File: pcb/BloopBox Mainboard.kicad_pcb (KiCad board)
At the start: 4 copper layers, 65 x 44 mm, 58 parts, among them J1 ExtLED, J2 SPKR, J3 Raspberry_Pi, J4 I2C, J5 NFC-Module, J6 GPIO, J7 TailBoard, J8 PROG, Q1 2N7002, Q2 2N7002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

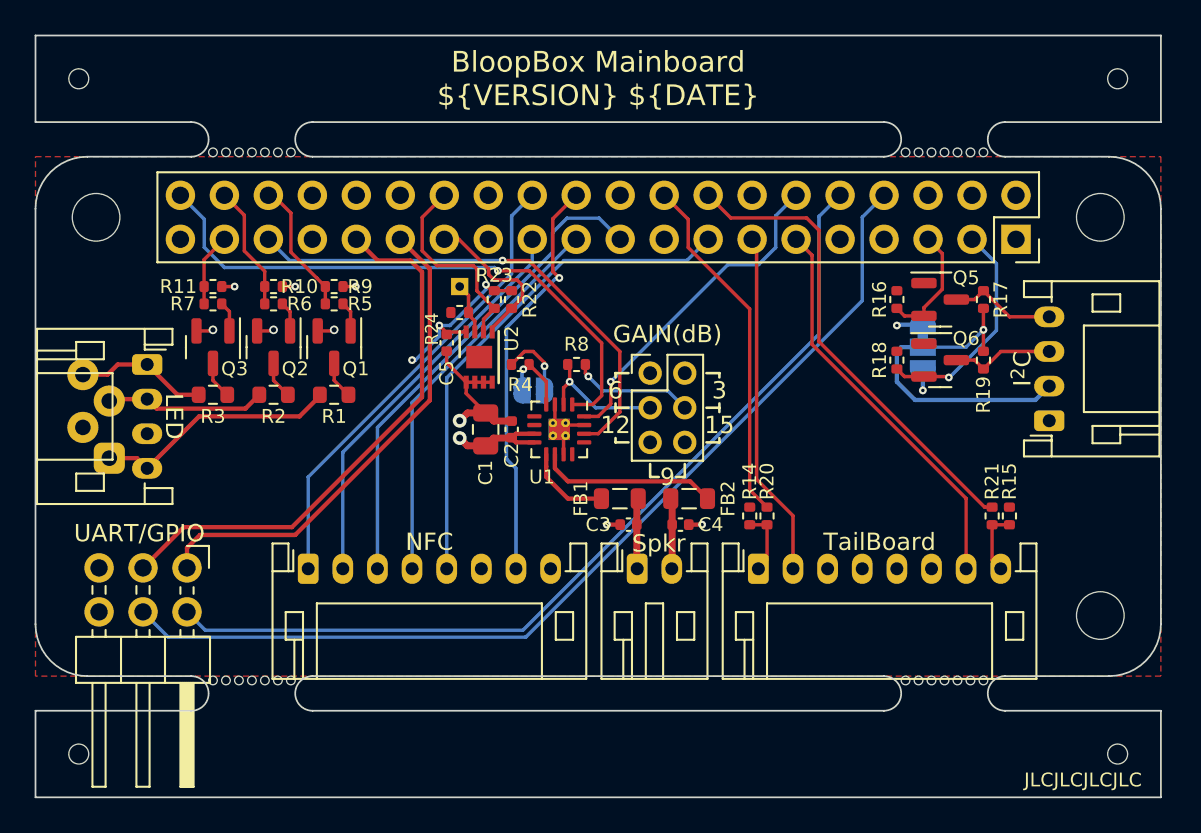
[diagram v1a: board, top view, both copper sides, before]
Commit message: feat!: remove RGB LED
remove the RGB LED facilities since we're using I2C for that now
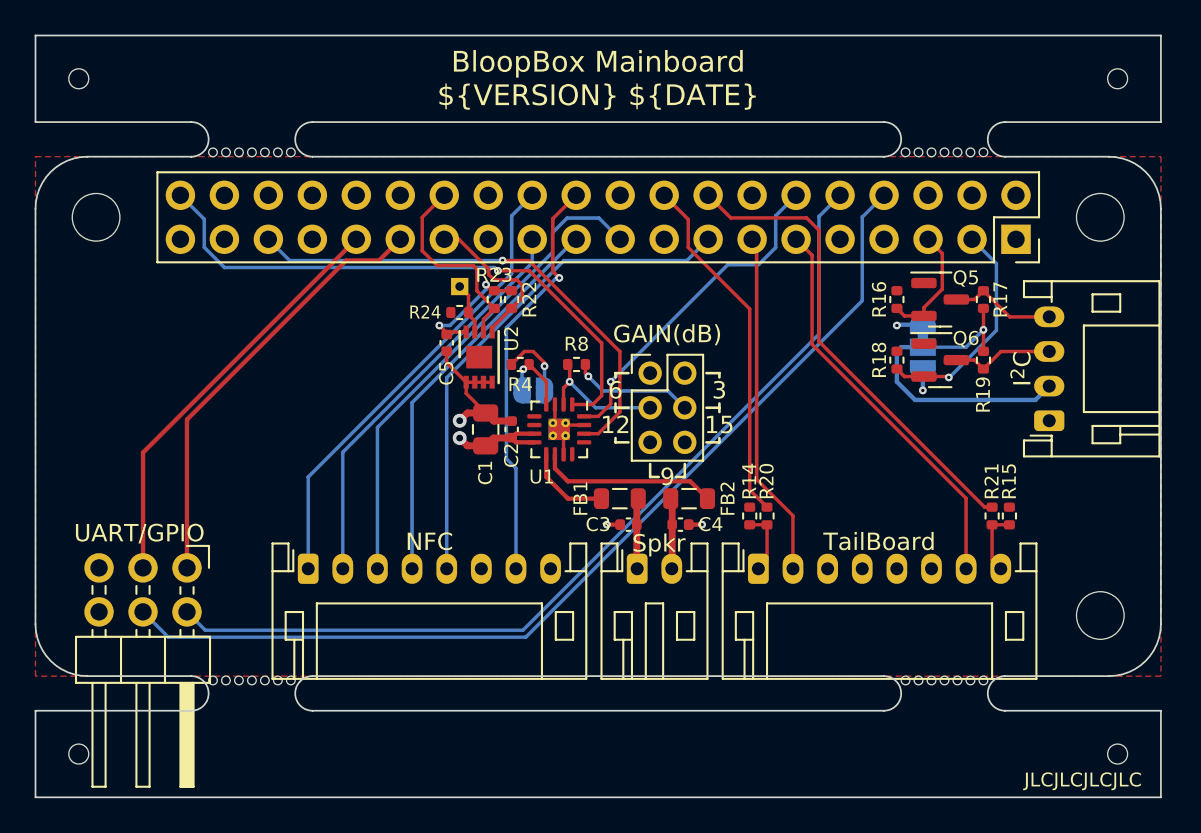
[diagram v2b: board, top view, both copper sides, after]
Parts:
- removed D1: LED_RAGB, LED_THT:LED_D5.0mm-4_RGB_Staggered_Pins
- removed J1: ExtLED, Connector_JST:JST_PH_S4B-PH-K_1x04_P2.00mm_Horizontal
- removed Q1, Q2, Q3: 2N7002, Package_TO_SOT_SMD:SOT-23
- removed R1: 300R, Resistor_SMD:R_0603_1608Metric
- removed R10, R11, R9: 10k, Resistor_SMD:R_0402_1005Metric
- removed R2, R3: 180R, Resistor_SMD:R_0603_1608Metric
- removed R5, R6, R7: 100R, Resistor_SMD:R_0402_1005Metric
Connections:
- J3 pad 36: /LED_RED -> unconnected-(J3-Pad36)
- J3 pad 37: /LED_BLUE -> unconnected-(J3-Pad37)
- J3 pad 38: /LED_GREEN -> unconnected-(J3-Pad38)
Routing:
- net /Rc: track 14.2 -> 0.00 mm
- net /Gc: track 9.27 -> 0.00 mm
- net /GPIO6: track 32.0 -> 24.1 mm
- net /LED_RED: track 7.80 -> 0.00 mm
- net /Bc: track 7.66 -> 0.00 mm
- net /LED_GREEN: track 7.24 -> 0.00 mm
- net GND: track 18.9 -> 13.8 mm, vias 9 -> 3
- net /LED_BLUE: track 4.21 -> 0.00 mm
- net /GPIO5: track 28.7 -> 25.2 mm
- net +3V3: track 11.4 -> 8.25 mm, vias 4 -> 3
- net /Rd: track 2.15 -> 0.00 mm
- net /Gd: track 2.15 -> 0.00 mm
- net /Bd: track 2.15 -> 0.00 mm
- net /Rg: track 1.74 -> 0.00 mm
- net /Gg: track 1.74 -> 0.00 mm
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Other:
- board text removed: "LED"

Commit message: style: remove disused silkscreen elements
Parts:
- moved G*** 2.95 mm to (133.2, 60.2)
- moved REF** 2.95 mm to (126.0, 61.0)
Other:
- board text removed: "+"
- board text removed: "B"
- board text removed: "G"
- board text removed: "R"
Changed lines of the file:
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@@
   )
   (footprint "Symbol:OSHW-Logo_5.7x6mm_SilkScreen" (layer "B.Cu")
-    (at 128.95 60.45 180)
+    (at 126.05 61 180)
     (descr "Open Source Hardware Logo")
     (tags "Logo OSHW")
@@
   )
   (footprint "My_Footprints:CutieMark5mmInverted" (layer "B.Cu")
-    (at 136.15 59.7 180)
+    (at 133.25 60.25 180)
     (attr through_hole board_only exclude_from_pos_files exclude_from_bom)
     (fp_text reference "G***" (at 0 0) (layer "B.SilkS") hide
@@
     (effects (font (size 1 1) (thickness 0.15)) (justify left mirror))
   )
-  (gr_text "G" (at 124.75 60.5) (layer "B.SilkS")
-    (effects (font (size 1 1) (thickness 0.15)) (justify right mirror))
-  )
   (gr_text "SEL" (at 133.25 71.5 90) (layer "B.SilkS")
     (effects (font (size 1 1) (thickness 0.15)) (justify left mirror))
@@
     (effects (font (size 1 1) (thickness 0.15)) (justify left mirror))
   )
-  (gr_text "+" (at 124.75 62.5) (layer "B.SilkS")
-    (effects (font (size 1 1) (thickness 0.15)) (justify right mirror))
-  )
   (gr_text "IO2" (at 171.25 71.5 90) (layer "B.SilkS")
     (effects (font (size 1 1) (thickness 0.15)) (justify left mirror))
@@
     (effects (font (size 1 1) (thickness 0.15)) (justify left mirror))
   )
-  (gr_text "B" (at 124.75 58.5) (layer "B.SilkS")
-    (effects (font (size 1 1) (thickness 0.15)) (justify right mirror))
-  )
   (gr_text "11" (at 135.25 69.25 90) (layer "B.SilkS")
     (effects (font (size 1 1) (thickness 0.15)) (justify right mirror))
   )
-  (gr_text "qete.sh/el" (at 136.15 62.95) (layer "B.SilkS")
+  (gr_text "qete.sh/el" (at 133.25 63.5) (layer "B.SilkS")
     (effects (font (size 1 1) (thickness 0.15)) (justify mirror))
   )
@@
     (effects (font (size 1 1) (thickness 0.15)) (justify left mirror))
   )
-  (gr_text "R" (at 124.75 64.5) (layer "B.SilkS")
-    (effects (font (size 1 1) (thickness 0.15)) (justify right mirror))
-  )
   (gr_text "27" (at 161.25 69.25 90) (layer "B.SilkS")

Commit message: feat: reduce to two layers
After removing some optional and deprecated hardware the board can be reduced to 2 layers to save production cost
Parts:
- removed JP3: SolderJumper_3_Bridged12, Jumper:SolderJumper-3_P1.3mm_Bridged12_RoundedPad1.0x1.5mm
- removed Q5, Q6: 2N7002, Package_TO_SOT_SMD:SOT-23
- removed R17, R19: 10k, Resistor_SMD:R_0402_1005Metric
- R16, R18: value 10k -> 4k7
- moved R16 4.85 mm to (172.0, 55.8), turned to 180 degrees
- moved R18 4.78 mm to (172.0, 57.8), turned to 180 degrees
- moved G*** 4.70 mm to (131.2, 56.0)
- moved REF** 4.70 mm to (124.0, 56.8)
- moved C5 3.75 mm to (137.5, 57.2)
- moved J8 3.75 mm to (138.2, 54.0)
- moved R22 3.75 mm to (141.2, 54.8)
- moved R23 3.75 mm to (140.2, 54.8)
- moved R24 3.75 mm to (138.2, 55.5)
- moved U2 3.75 mm to (139.4, 58.1)
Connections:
- J4 pad 2: /V_I2C -> +3V3
- J4 pad 3: /SDA_OUT -> /SDA
- J4 pad 4: /SCL_OUT -> /SCL
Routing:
- net /V_I2C: track 19.3 -> 0.00 mm, vias 1 -> 0
- net /AMP_LRCLK: track 29.1 -> 39.1 mm
- net /SCL_OUT: track 6.20 -> 0.00 mm
- net /SDA_OUT: track 5.99 -> 0.00 mm
- net GND: track 13.8 -> 8.33 mm, vias 3 -> 0
- net /ID_SD: track 8.97 -> 6.26 mm
- net /SDA: track 12.9 -> 10.4 mm
- net /SCL: track 6.96 -> 9.45 mm
- net /ID_SC: track 11.6 -> 9.37 mm
- net /TX: track 56.8 -> 57.8 mm
- net /RX: track 52.5 -> 53.5 mm
- net +5V: track 11.8 -> 11.1 mm, vias 3 -> 2
- net +3V3: track 8.25 -> 8.26 mm, vias 3 -> 5
- added copper zone on B.Cu, net +3V3
- added copper zone on B.Cu, net +5V
- added copper zone on F.Cu, net GND
- removed copper zone on F.Cu, net +3V3
- removed copper zone on In2.Cu, net +5V
- removed copper zone on In1.Cu, net GND
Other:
- copper layers 4 -> 2
- board text removed: "5V 3V3"
- board text removed: "I2C Voltage"

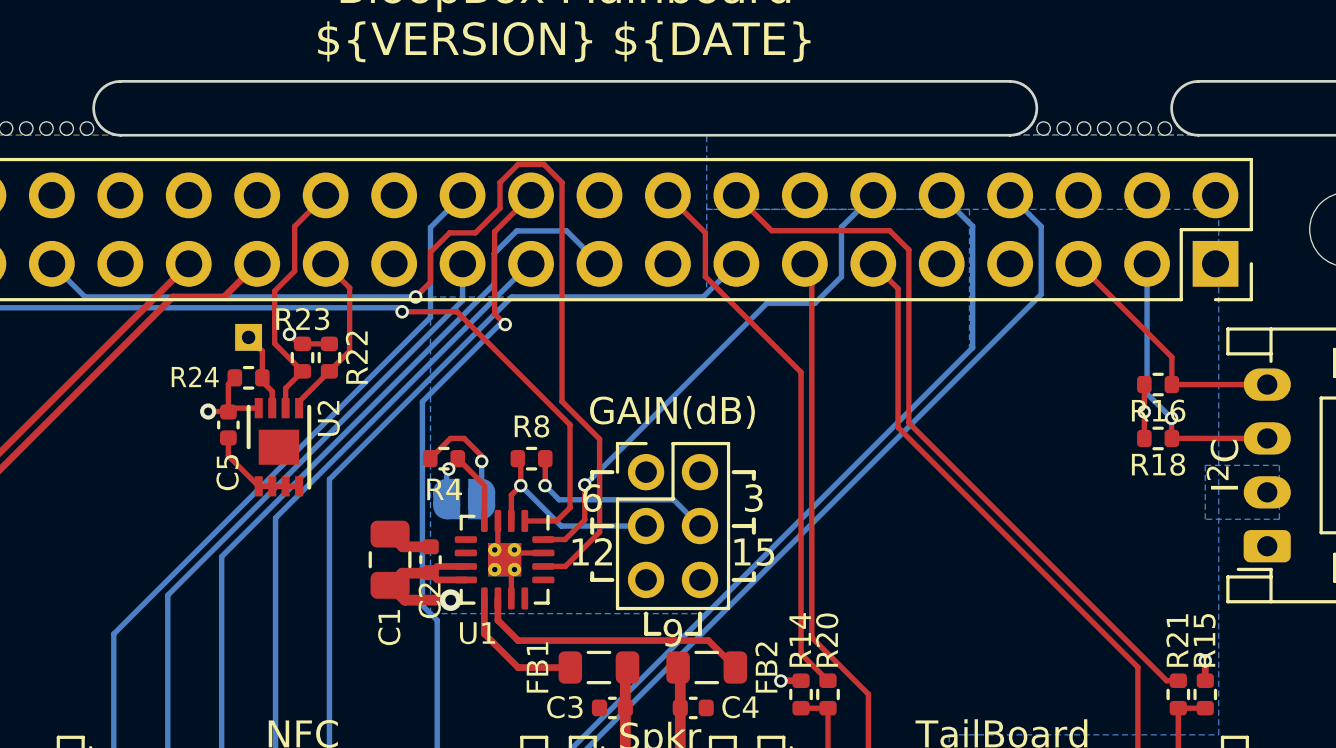
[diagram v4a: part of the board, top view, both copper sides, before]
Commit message: feat!: remove HAT EEPROM
Since it is more effort to program each EEPROM after assembly than manually changing the settings it could handle, the EEPROM would only be a novelty and was removed.
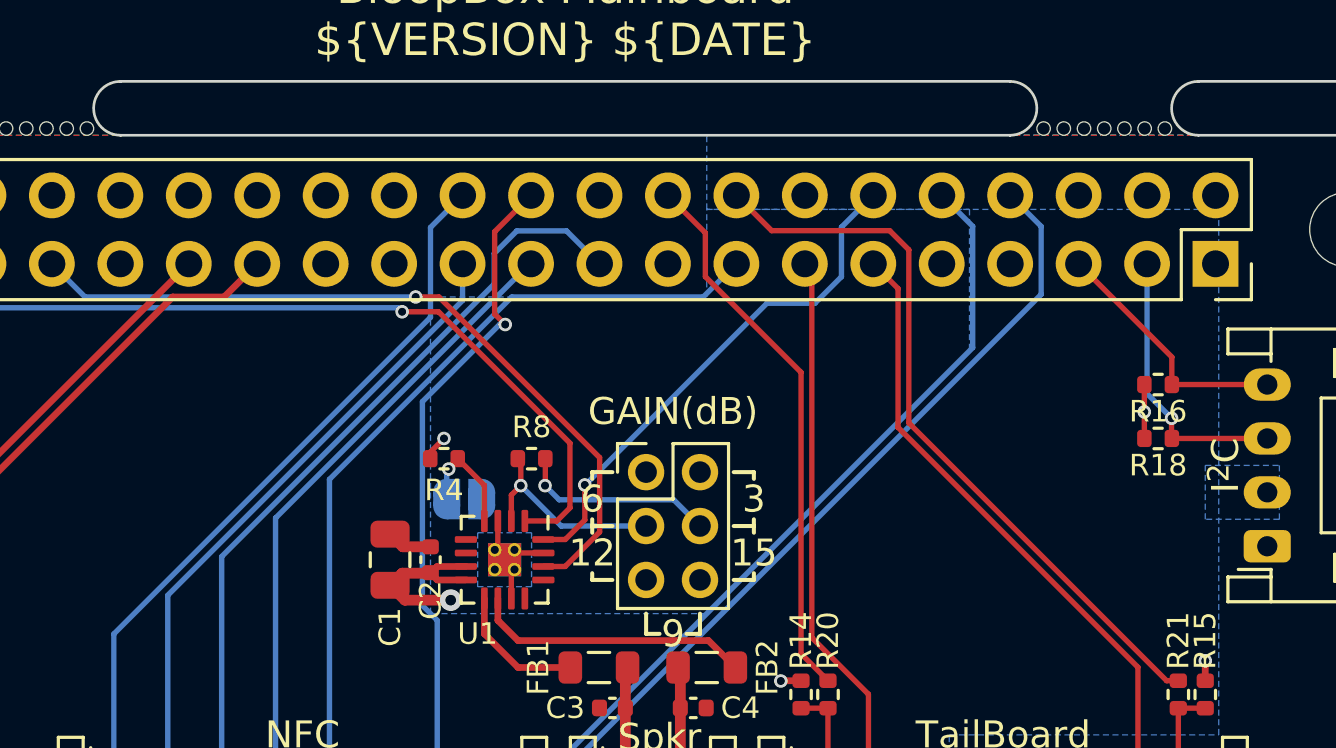
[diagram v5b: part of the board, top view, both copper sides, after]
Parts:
- removed C5: 100nF, Capacitor_SMD:C_0402_1005Metric
- removed J8: PROG, TestPoint:TestPoint_THTPad_1.0x1.0mm_Drill0.5mm
- removed R22, R23: 3k9, Resistor_SMD:R_0402_1005Metric
- removed R24: 1k, Resistor_SMD:R_0402_1005Metric
- removed U2: CAT24C32, Package_DFN_QFN:DFN-8-1EP_3x2mm_P0.5mm_EP1.3x1.5mm
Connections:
- J3 pad 27: /ID_SD -> unconnected-(J3-Pad27)
- J3 pad 28: /ID_SC -> unconnected-(J3-Pad28)
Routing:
- net /AMP_LRCLK: track 39.1 -> 28.7 mm
- net /ID_SC: track 9.37 -> 0.00 mm
- net /ID_SD: track 6.26 -> 0.00 mm
- net +3V3: track 8.26 -> 3.50 mm, vias 5 -> 3
- net GND: track 8.33 -> 4.57 mm
- net +5V: track 11.1 -> 7.96 mm
- net /ID_WP: track 2.99 -> 0.00 mm
- added copper zone on B.Cu, net GND
